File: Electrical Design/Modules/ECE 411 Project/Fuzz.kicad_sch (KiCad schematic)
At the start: 11 parts, among them Q5 PNP, Q6 PNP

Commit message: kicad business
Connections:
- net Input renamed FUZZIN
- net Output renamed FUZZOUT
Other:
- company: (none) -> Portland State University
- title: (none) -> Fuzz & Distortion Effect
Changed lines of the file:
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@@
 	(generator_version "8.0")
 	(paper "A4")
-	(junction
-		(at 106.68 48.26)
-		(diameter 0)
-		(color 0 0 0 0)
+	(title_block
+		(title "Fuzz & Distortion Effect")
+		(date "2024-10-31")
+		(rev "1.1")
+		(company "Portland State University")
+		(comment 1 "Open Source Hardware")
+		(comment 2 "Design: Eric Sanman, Sierra Buckley, Chuong Vo, Chris Crider")
 	)
 	(junction
@@
 	(wire
 		(pts
-			(xy 106.68 48.26) (xy 114.3 48.26)
-		)
-		(stroke
-			(width 0)
-			(type default)
-		)
-	)
-	(wire
-		(pts
 			(xy 107.95 85.09) (xy 96.52 85.09)
 		)
@@
 	(wire
 		(pts
-			(xy 83.82 48.26) (xy 83.82 55.88)
-		)
-		(stroke
-			(width 0)
-			(type default)
-		)
-	)
-	(wire
-		(pts
 			(xy 96.52 69.85) (xy 96.52 57.15)
 		)
@@
 	(wire
 		(pts
-			(xy 114.3 46.99) (xy 114.3 48.26)
-		)
-		(stroke
-			(width 0)
-			(type default)
-		)
-	)
-	(wire
-		(pts
 			(xy 115.57 118.11) (xy 115.57 127)
 		)
@@
 	(wire
 		(pts
-			(xy 106.68 48.26) (xy 83.82 48.26)
-		)
-		(stroke
-			(width 0)
-			(type default)
-		)
-	)
-	(wire
-		(pts
 			(xy 107.95 90.17) (xy 107.95 85.09)
 		)
@@
 		)
 	)
-	(global_label "9V"
+	(hierarchical_label "-9V"
 		(shape input)
-		(at 83.82 55.88 180)
+		(at 106.68 48.26 90)
 		(fields_autoplaced yes)
 		(effects
@@
 				(size 1.27 1.27)
 			)
-			(justify right)
-		)
-		(property "Intersheetrefs" "${INTERSHEET_REFS}"
-			(at 78.5367 55.88 0)
-			(effects
-				(font
-					(size 1.27 1.27)
-				)
-				(justify right)
-				(hide yes)
-			)
-		)
-	)
-	(global_label "Input"
+			(justify left)
+		)
+	)
+	(hierarchical_label "FUZZIN"
 		(shape input)
 		(at 58.42 90.17 180)
@@
 			(justify right)
 		)
-		(property "Intersheetrefs" "${INTERSHEET_REFS}"
-			(at 50.6573 90.17 0)
-			(effects
-				(font
-					(size 1.27 1.27)
-				)
-				(justify right)
-				(hide yes)
-			)
-		)
-	)
-	(global_label "Output"
-		(shape input)
+	)
+	(hierarchical_label "FUZZOUT"
+		(shape output)
 		(at 162.56 76.2 0)
 		(fields_autoplaced yes)
@@
 			(justify left)
 		)
-		(property "Intersheetrefs" "${INTERSHEET_REFS}"
-			(at 171.7741 76.2 0)
-			(effects
-				(font
-					(size 1.27 1.27)
-				)
-				(justify left)
-				(hide yes)
-			)
-		)
-	)
-	(global_label "-9V"
-		(shape input)
-		(at 114.3 46.99 90)
-		(fields_autoplaced yes)
-		(effects
-			(font
-				(size 1.27 1.27)
-			)
-			(justify left)
-		)
-		(property "Intersheetrefs" "${INTERSHEET_REFS}"
-			(at 114.3 40.1343 90)
-			(effects
-				(font
-					(size 1.27 1.27)
-				)
-				(justify left)
-				(hide yes)
-			)
-		)
-	)
+	)

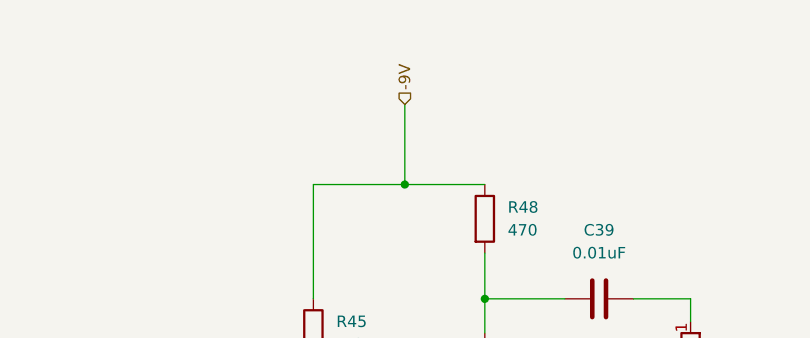
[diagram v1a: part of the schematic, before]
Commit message: add psu and fix schematic
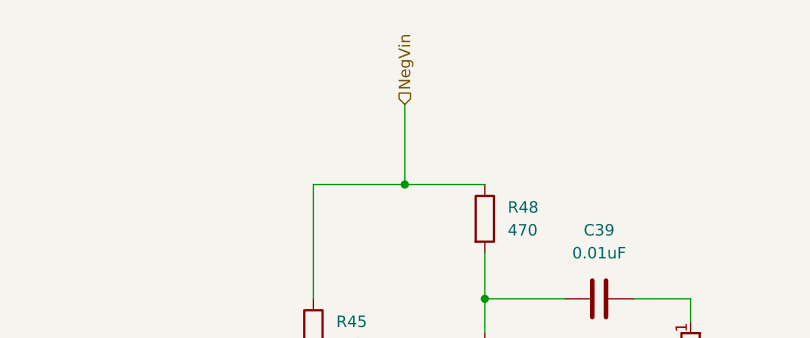
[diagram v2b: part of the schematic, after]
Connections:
- net -9V renamed NegVin
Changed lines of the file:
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@@
 		)
 	)
-	(hierarchical_label "-9V"
+	(hierarchical_label "NegVin"
 		(shape input)
 		(at 106.68 48.26 90)

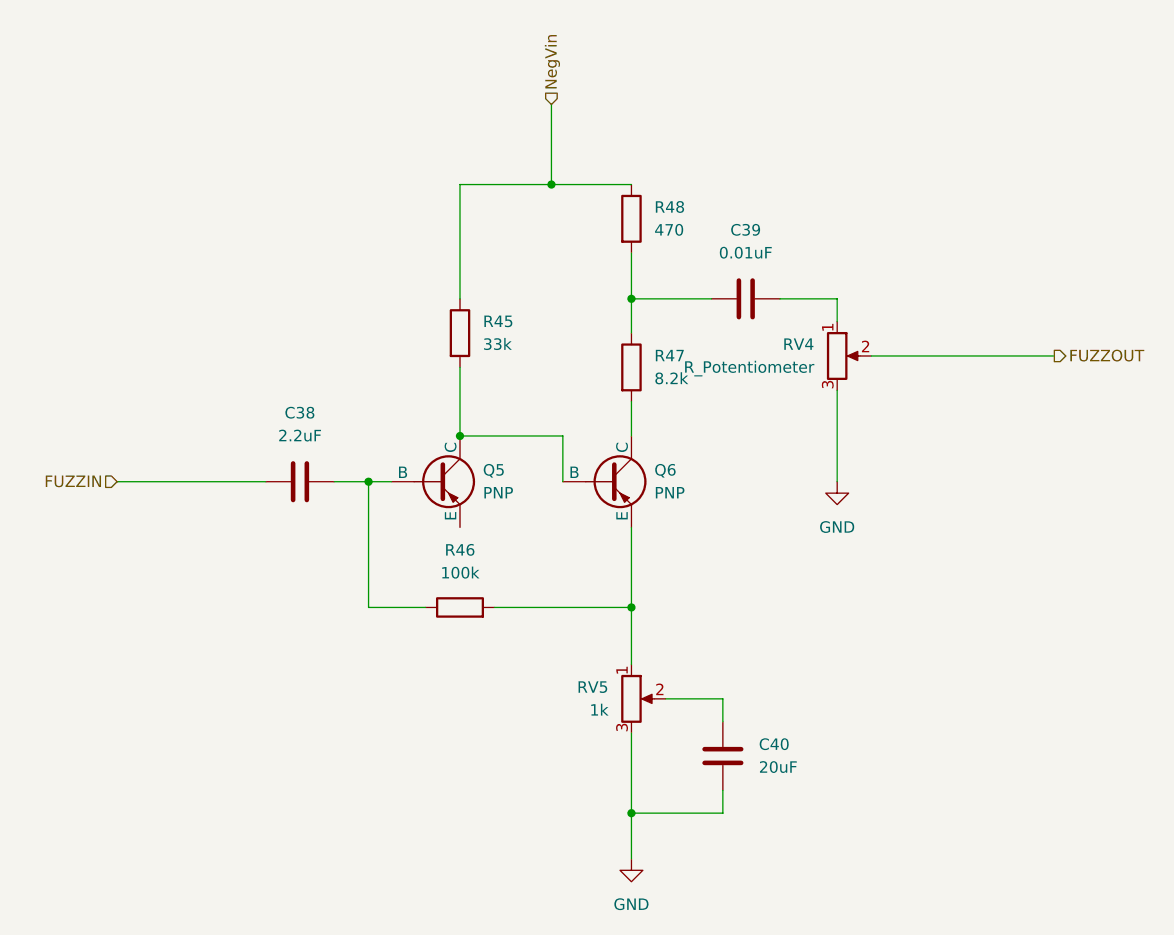
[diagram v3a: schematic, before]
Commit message: schematic, start layout
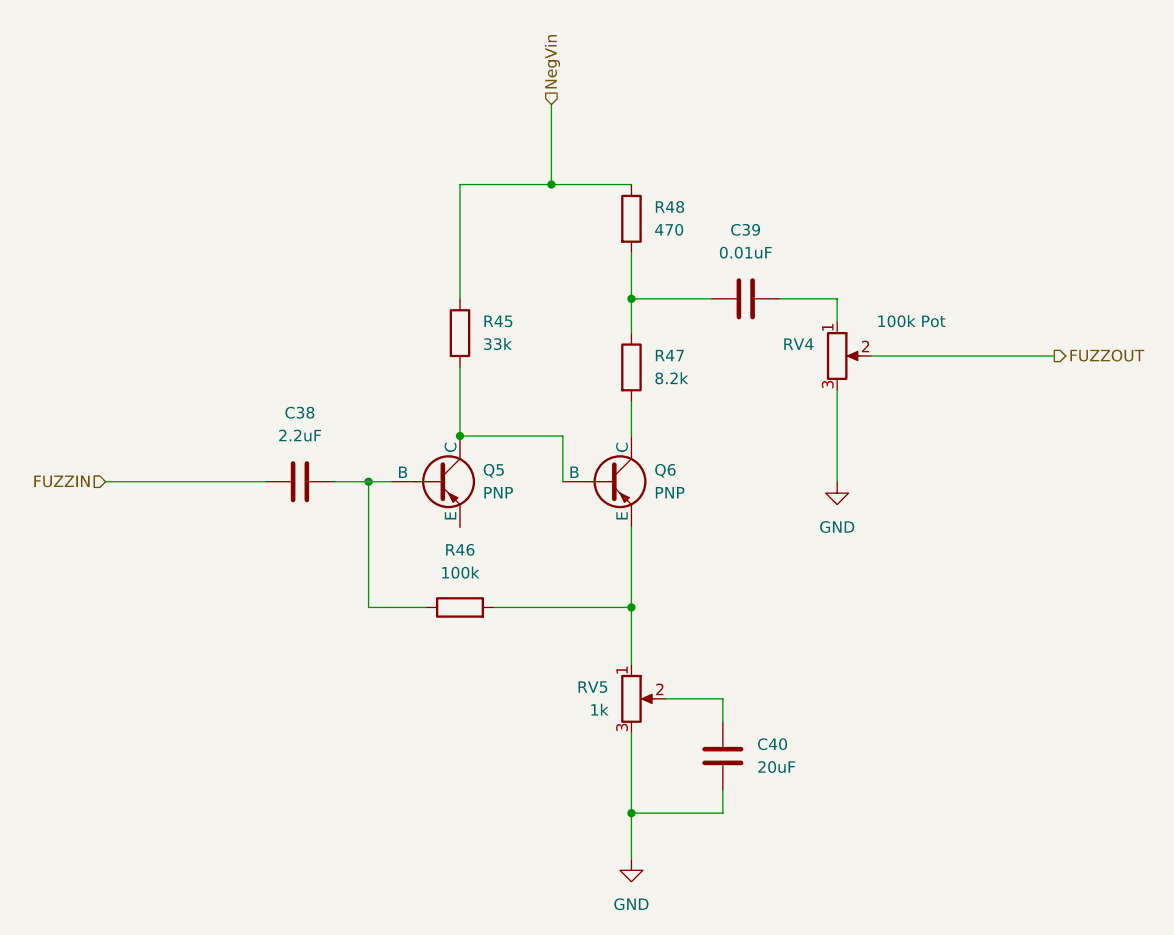
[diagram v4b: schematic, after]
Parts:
- C38, C39: footprint (none) -> Capacitor_SMD:C_0805_2012Metric_Pad1.18x1.45mm_HandSolder
- C40: footprint (none) -> Capacitor_SMD:C_1206_3216Metric_Pad1.33x1.80mm_HandSolder
- Q5, Q6: footprint (none) -> Package_TO_SOT_THT:TO-52-3
- R45, R46, R47, R48: footprint (none) -> Resistor_SMD:R_0805_2012Metric_Pad1.20x1.40mm_HandSolder
- RV4: value R_Potentiometer -> 100k Pot; footprint (none) -> Connector_PinHeader_2.54mm:PinHeader_1x03_P2.54mm_Vertical
- RV5: footprint (none) -> Connector_PinHeader_2.54mm:PinHeader_1x03_P2.54mm_Vertical
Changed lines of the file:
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@@
 	(title_block
 		(title "Fuzz & Distortion Effect")
-		(date "2024-10-31")
-		(rev "1.1")
+		(date "2024-11-07")
+		(rev "1.5")
 		(company "Portland State University")
 		(comment 1 "Open Source Hardware")
@@
 	(wire
 		(pts
-			(xy 58.42 90.17) (xy 74.93 90.17)
-		)
-		(stroke
-			(width 0)
-			(type default)
-		)
-	)
-	(wire
-		(pts
 			(xy 142.24 76.2) (xy 162.56 76.2)
 		)
@@
 		(pts
 			(xy 106.68 57.15) (xy 115.57 57.15)
+		)
+		(stroke
+			(width 0)
+			(type default)
+		)
+	)
+	(wire
+		(pts
+			(xy 57.15 90.17) (xy 74.93 90.17)
 		)
 		(stroke
@@
 	(hierarchical_label "FUZZIN"
 		(shape input)
-		(at 58.42 90.17 180)
+		(at 57.15 90.17 180)
 		(fields_autoplaced yes)
 		(effects
@@
 			)
 		)
-		(property "Footprint" ""
+		(property "Footprint" "Package_TO_SOT_THT:TO-52-3"
 			(at 129.54 90.17 0)
 			(effects
@@
 		(on_board yes)
 		(dnp no)
-		(fields_autoplaced yes)
 		(property "Reference" "RV4"
 			(at 135.89 74.9299 0)
@@
 			)
 		)
-		(property "Value" "R_Potentiometer"
-			(at 135.89 77.4699 0)
+		(property "Value" "100k Pot"
+			(at 150.495 72.39 0)
 			(effects
 				(font
@@
 			)
 		)
-		(property "Footprint" ""
+		(property "Footprint" "Connector_PinHeader_2.54mm:PinHeader_1x03_P2.54mm_Vertical"
 			(at 138.43 76.2 0)
 			(effects
@@
 			)
 		)
-		(property "Footprint" ""
+		(property "Footprint" "Capacitor_SMD:C_0805_2012Metric_Pad1.18x1.45mm_HandSolder"
 			(at 82.55 89.2048 0)
 			(effects
@@
 			)
 		)
-		(property "Footprint" ""
+		(property "Footprint" "Capacitor_SMD:C_0805_2012Metric_Pad1.18x1.45mm_HandSolder"
 			(at 132.08 68.8848 0)
 			(effects
@@
 		(fields_autoplaced yes)
 		(property "Reference" "C40"
-			(at 129.7216 119.3799 0)
+			(at 129.54 119.3799 0)
 			(effects
 				(font
@@
 		)
 		(property "Value" "20uF"
-			(at 129.7216 121.9199 0)
+			(at 129.54 121.9199 0)
 			(effects
 				(font
@@
 			)
 		)
-		(property "Footprint" ""
+		(property "Footprint" "Capacitor_SMD:C_1206_3216Metric_Pad1.33x1.80mm_HandSolder"
 			(at 124.7648 116.84 0)
 			(effects
@@
 			)
 		)
-		(property "Footprint" ""
+		(property "Footprint" "Connector_PinHeader_2.54mm:PinHeader_1x03_P2.54mm_Vertical"
 			(at 115.57 114.3 0)
 			(effects
@@
 			)
 		)
-		(property "Footprint" ""
+		(property "Footprint" "Package_TO_SOT_THT:TO-52-3"
 			(at 148.59 90.17 0)
 			(effects
@@
 			)
 		)
-		(property "Footprint" ""
+		(property "Footprint" "Resistor_SMD:R_0805_2012Metric_Pad1.20x1.40mm_HandSolder"
 			(at 94.742 73.66 90)
 			(effects
@@
 			)
 		)
-		(property "Footprint" ""
+		(property "Footprint" "Resistor_SMD:R_0805_2012Metric_Pad1.20x1.40mm_HandSolder"
 			(at 96.52 105.918 90)
 			(effects
@@
 			)
 		)
-		(property "Footprint" ""
+		(property "Footprint" "Resistor_SMD:R_0805_2012Metric_Pad1.20x1.40mm_HandSolder"
 			(at 113.792 60.96 90)
 			(effects
@@
 			)
 		)
-		(property "Footprint" ""
+		(property "Footprint" "Resistor_SMD:R_0805_2012Metric_Pad1.20x1.40mm_HandSolder"
 			(at 113.792 77.47 90)
 			(effects

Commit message: update kicad
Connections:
- net GND: now also Q5.3 (E)
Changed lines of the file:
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@@
+	(wire
+		(pts
+			(xy 96.52 95.885) (xy 104.775 95.885)
+		)
+		(stroke
+			(width 0)
+			(type default)
+		)
+	)
 	(wire
 		(pts
@@
 	(wire
 		(pts
+			(xy 104.775 95.885) (xy 104.775 96.52)
+		)
+		(stroke
+			(width 0)
+			(type default)
+		)
+	)
+	(wire
+		(pts
 			(xy 82.55 90.17) (xy 86.36 90.17)
 		)
@@
 		(pts
 			(xy 119.38 114.3) (xy 125.73 114.3)
+		)
+		(stroke
+			(width 0)
+			(type default)
+		)
+	)
+	(wire
+		(pts
+			(xy 96.52 95.25) (xy 96.52 95.885)
 		)
 		(stroke
@@
 					(unit 1)
 				)
+			)
+		)
+	)
+	(symbol
+		(lib_id "power:GND")
+		(at 104.775 96.52 0)
+		(unit 1)
+		(exclude_from_sim no)
+		(in_bom yes)
+		(on_board yes)
+		(dnp no)
+		(fields_autoplaced yes)
+		(property "Reference" "#PWR011"
+			(at 104.775 102.87 0)
+			(effects
+				(font
+					(size 1.27 1.27)
+				)
+				(hide yes)
+			)
+		)
+		(property "Value" "GND"
+			(at 104.775 101.6 0)
+			(effects
+				(font
+					(size 1.27 1.27)
+				)
+			)
+		)
+		(property "Footprint" ""
+			(at 104.775 96.52 0)
+			(effects
+				(font
+					(size 1.27 1.27)
+				)
+				(hide yes)
+			)
+		)
+		(property "Datasheet" ""
+			(at 104.775 96.52 0)
+			(effects
+				(font
+					(size 1.27 1.27)
+				)
+				(hide yes)
+			)
+		)
+		(property "Description" "Power symbol creates a global label with name \"GND\" , ground"
+			(at 104.775 96.52 0)
+			(effects
+				(font
+					(size 1.27 1.27)
+				)
+				(hide yes)
+			)
+		)
+		(pin "1"
+		)
+		(instances
+			(project ""
+				(path "/2625e5a1-d0c8-41ce-941d-75d035a5f1c5/3d12698d-f95b-4276-b064-730c4280216d"
+					(reference "#PWR011")
+					(unit 1)
+				)

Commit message: update BOM
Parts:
- C38, C40, R45, R46, R47, R48: Part Origin (none) -> DK
- C39: value 0.01uF -> 10nF; Part Origin (none) -> DK
- RV4, RV5: Part Origin (none) -> AMZ

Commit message: update kicad
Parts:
- C40: value 20uF -> 22uF
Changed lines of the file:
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@@
 			)
 		)
-		(property "Value" "20uF"
+		(property "Value" "22uF"
 			(at 129.54 121.9199 0)
 			(effects
